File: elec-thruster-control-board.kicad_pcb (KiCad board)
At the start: 2 copper layers, 70 x 69 mm, 50 parts, among them J11 gp17-pwm0B, J12 gp2-pwm1A, J13 Conn_01x07, J15 gp6-pwm3A, J16 gp8-pwm4A, J18 gp19-pwm1B, J19 gp21-pwm2B, J2 gp0-pwm0A, J20 gp26-pwm5A, J21 gp27-pwm5B, J22 Conn_01x06, J24 Conn_01x06, J5 gp4-pwm2A

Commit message: This is the true final edition of this project
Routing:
- net /gp17-pwm0B: track 38.6 -> 52.9 mm
- net /gp0-pwm0A: track 40.4 -> 47.3 mm
- net /gp8-pwm4A: track 47.7 -> 48.2 mm
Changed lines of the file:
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@@
+	)
+	(segment
+		(start 163.58 81.58)
+		(end 164.75 82.75)
+		(width 0.4)
+		(layer "F.Cu")
+		(net 1)
 	)
 	(segment
@@
 	)
 	(segment
+		(start 164.75 92.25)
+		(end 162.5 94.5)
+		(width 0.4)
+		(layer "F.Cu")
+		(net 1)
+	)
+	(segment
+		(start 164.75 82.75)
+		(end 164.75 92.25)
+		(width 0.4)
+		(layer "F.Cu")
+		(net 1)
+	)
+	(segment
+		(start 162.5 94.5)
+		(end 150.6925 94.5)
+		(width 0.4)
+		(layer "F.Cu")
+		(net 1)
+	)
+	(segment
 		(start 151.285 96.715)
 		(end 152.5 95.5)
@@
 	)
 	(segment
-		(start 164.75 82.75)
+		(start 150.6925 94.5)
+		(end 148.4775 96.715)
+		(width 0.4)
+		(layer "F.Cu")
+		(net 1)
+	)
+	(segment
+		(start 162.25 81.58)
 		(end 163.58 81.58)
-		(width 0.4)
-		(layer "F.Cu")
-		(net 1)
-	)
-	(segment
-		(start 163.58 81.58)
-		(end 162.25 81.58)
 		(width 0.4)
 		(layer "F.Cu")
@@
 	)
 	(segment
-		(start 164.75 82.75)
-		(end 164.75 94)
-		(width 0.4)
-		(layer "F.Cu")
-		(net 1)
-	)
-	(segment
-		(start 164.75 94)
-		(end 163.25 95.5)
-		(width 0.4)
-		(layer "F.Cu")
-		(net 1)
-	)
-	(segment
 		(start 151.495 99.255)
 		(end 148.4775 99.255)
@@
 	(segment
 		(start 125.25 88.75)
-		(end 119.5 88.75)
+		(end 120.75 88.75)
 		(width 0.4)
 		(layer "F.Cu")
@@
 	(segment
 		(start 119.5 88.75)
-		(end 119.5 82.5)
+		(end 119.5 87.5)
 		(width 0.4)
 		(layer "F.Cu")
@@
 	)
 	(segment
+		(start 120.75 88.75)
+		(end 119.5 87.5)
+		(width 0.4)
+		(layer "F.Cu")
+		(net 6)
+	)
+	(segment
 		(start 127 87)
 		(end 125.25 88.75)
@@
 	)
 	(segment
+		(start 119.5 87.5)
+		(end 119.5 82.5)
+		(width 0.4)
+		(layer "F.Cu")
+		(net 6)
+	)
+	(segment
 		(start 127 80.5)
 		(end 127 87)
@@
 	)
 	(segment
+		(start 114.75 62)
+		(end 115.75 63)
+		(width 0.4)
+		(layer "F.Cu")
+		(net 7)
+	)
+	(segment
 		(start 116.75 60.5)
 		(end 116.75 70.46)
@@
 	)
 	(segment
-		(start 116.75 61)
-		(end 115.75 62)
-		(width 0.4)
-		(layer "F.Cu")
-		(net 7)
-	)
-	(segment
-		(start 115.75 62)
-		(end 109.75 62)
+		(start 109.75 62)
+		(end 114.75 62)
 		(width 0.4)
 		(layer "F.Cu")
@@
 	)
 	(segment
+		(start 115.75 69.46)
+		(end 116.75 70.46)
+		(width 0.4)
+		(layer "F.Cu")
+		(net 7)
+	)
+	(segment
 		(start 118.255 50.995)
 		(end 116.75 52.5)
@@
 	)
 	(segment
+		(start 115.75 63)
+		(end 115.75 69.46)
+		(width 0.4)
+		(layer "F.Cu")
+		(net 7)
+	)
+	(segment
 		(start 149.765 66.235)
 		(end 148.4775 66.235)
@@
 		(start 155.5 72)
 		(end 156.4375 72)
-		(width 0.2)
+		(width 0.4)
 		(layer "F.Cu")
 		(net 10)
@@
 		(start 156.4375 72)
 		(end 157.5 73.0625)
-		(width 0.2)
+		(width 0.4)
 		(layer "F.Cu")
 		(net 10)
@@
 	)
 	(segment
+		(start 164.54 79.04)
+		(end 165.5 80)
+		(width 0.4)
+		(layer "F.Cu")
+		(net 16)
+	)
+	(segment
 		(start 150.405 89.095)
 		(end 153.25 86.25)
@@
 	)
 	(segment
+		(start 162.25 79.04)
+		(end 164.54 79.04)
+		(width 0.4)
+		(layer "F.Cu")
+		(net 16)
+	)
+	(segment
 		(start 158.5 86.25)
 		(end 159.75 85)
@@
 	)
 	(segment
+		(start 161.21 79.04)
+		(end 162.25 79.04)
+		(width 0.4)
+		(layer "F.Cu")
+		(net 16)
+	)
+	(segment
+		(start 167 86.75)
+		(end 170.25 86.75)
+		(width 0.4)
+		(layer "F.Cu")
+		(net 16)
+	)
+	(segment
 		(start 165.5 85.25)
 		(end 167 86.75)
@@
 	)
 	(segment
-		(start 161.21 79.04)
-		(end 162.25 79.04)
-		(width 0.4)
-		(layer "F.Cu")
-		(net 16)
-	)
-	(segment
-		(start 165.04 79.04)
-		(end 165.5 79.5)
+		(start 165.5 80)
+		(end 165.5 85.25)
 		(width 0.4)
 		(layer "F.Cu")
@@
 	)
 	(segment
-		(start 162.25 79.04)
-		(end 165.04 79.04)
-		(width 0.4)
-		(layer "F.Cu")
-		(net 16)
-	)
-	(segment
 		(start 148.4775 89.095)
 		(end 150.405 89.095)
@@
 	)
 	(segment
-		(start 165.5 79.5)
-		(end 165.5 85.25)
-		(width 0.4)
-		(layer "F.Cu")
-		(net 16)
-	)
-	(segment
-		(start 167 86.75)
-		(end 170.25 86.75)
-		(width 0.4)
-		(layer "F.Cu")
-		(net 16)
-	)
-	(segment
 		(start 134.015 84.015)
 		(end 146.75 96.75)
@@
 	)
 	(segment
+		(start 151.0425 68.75)
+		(end 159.58 68.75)
+		(width 0.4)
+		(layer "F.Cu")
+		(net 25)
+	)
+	(segment
+		(start 162.25 71.42)
+		(end 159.58 68.75)
+		(width 0.4)
+		(layer "F.Cu")
+		(net 25)
+	)
+	(segment
 		(start 162.25 65.75)
 		(end 162.25 71.42)
@@
 	(segment
 		(start 148.4775 71.315)
-		(end 154.0425 65.75)
-		(width 0.4)
-		(layer "F.Cu")
-		(net 25)
-	)
-	(segment
-		(start 154.0425 65.75)
-		(end 162.25 65.75)
+		(end 151.0425 68.75)
 		(width 0.4)
 		(layer "F.Cu")
@@
 	)
 	(segment
-		(start 157.475 75.9125)
-		(end 157.5 75.9375)
-		(width 0.2)
-		(layer "F.Cu")
-		(net 41)
-	)
-	(segment
 		(start 153.75 74.9125)
 		(end 157.475 74.9125)
-		(width 0.2)
+		(width 0.4)
 		(layer "F.Cu")
 		(net 41)

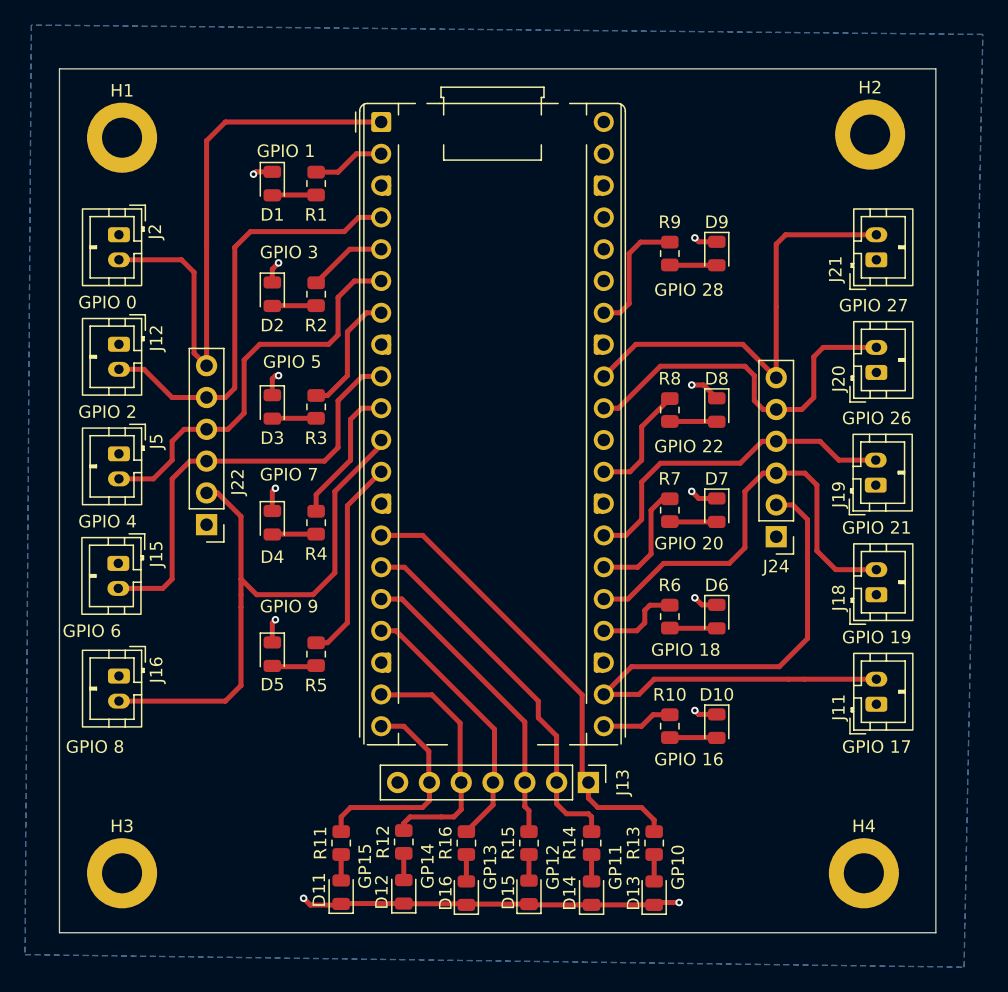
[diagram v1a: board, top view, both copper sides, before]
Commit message: Updated footprints in the schematic and pcb design. Also cleaned up some of the routing.
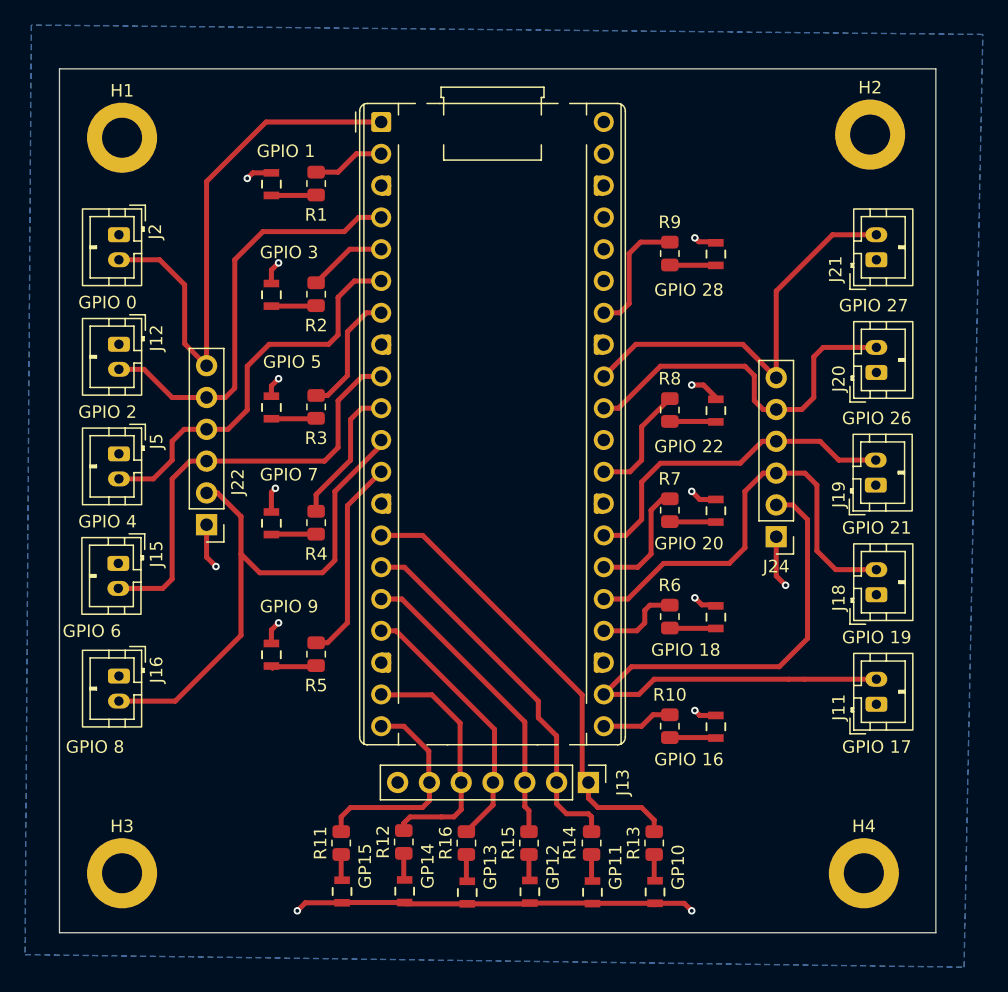
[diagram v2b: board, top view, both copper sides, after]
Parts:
- D1, D10, D11, D12, D13, D14, D15, D16, D2, D3, D4, D5, D6, D7, D8, D9: footprint LED_SMD:LED_0805_2012Metric -> Imported Footprints:LED_APT2012LZGCK
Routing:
- net GND: track 50.0 -> 60.1 mm, vias 12 -> 14
- net /gp8-pwm4A: track 48.2 -> 44.6 mm
- net /gp0-pwm0A: track 47.3 -> 43.9 mm
- net /gp27-pwm5B: track 34.9 -> 32.7 mm
- net Net-(D3-A): track 4.26 -> 3.62 mm
- net Net-(D2-A): track 4.26 -> 3.62 mm
- net /gp2-pwm1A: track 34.4 -> 33.8 mm

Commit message: Final PCB Design after design review Updated dimensions of board and mounting hole distance Fixed LED footprint Added Measurement values
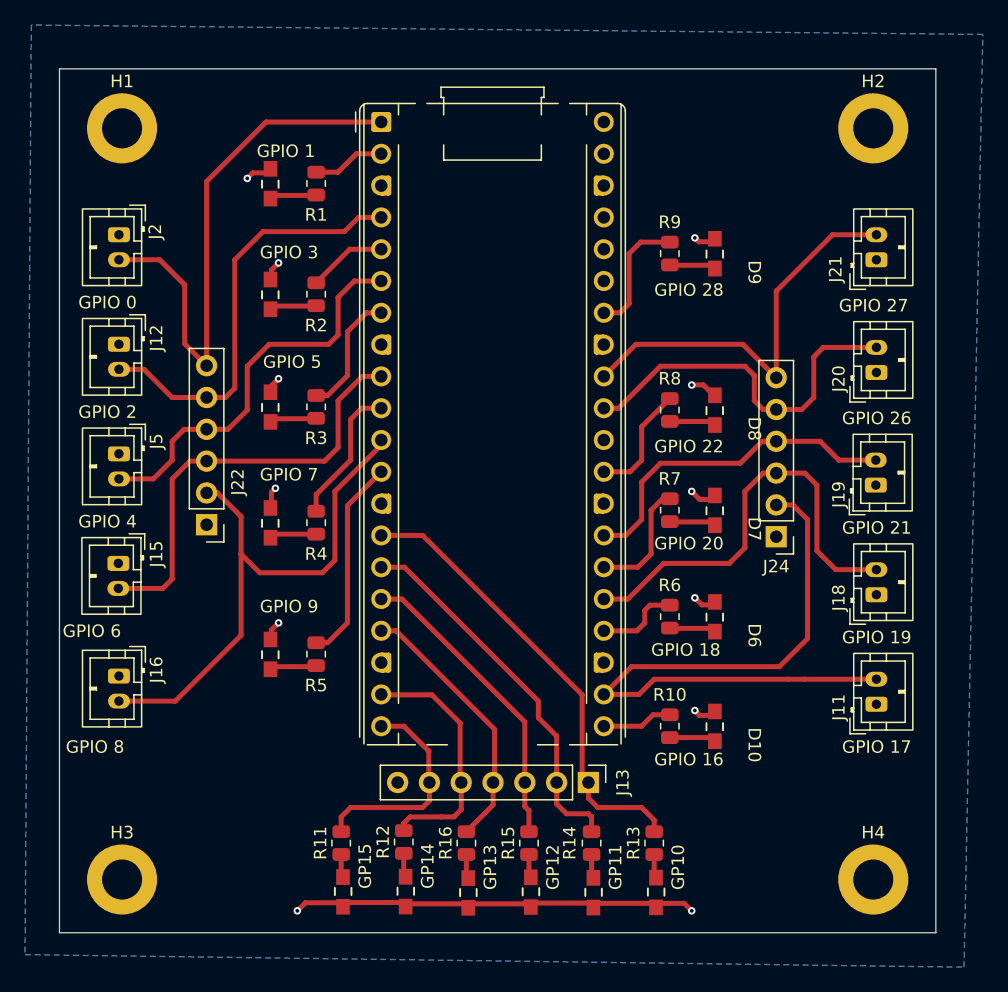
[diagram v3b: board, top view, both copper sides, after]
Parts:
- moved H4 0.90 mm to (170.0, 111.5)
- moved H1 0.75 mm to (110.0, 51.5)
- moved H2 0.56 mm to (170.0, 51.5)
- moved H3 0.50 mm to (110.0, 111.5)
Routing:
- net GND: track 60.1 -> 52.3 mm, vias 14 -> 12

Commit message: Added Labels for LEDs, and corrected Labels
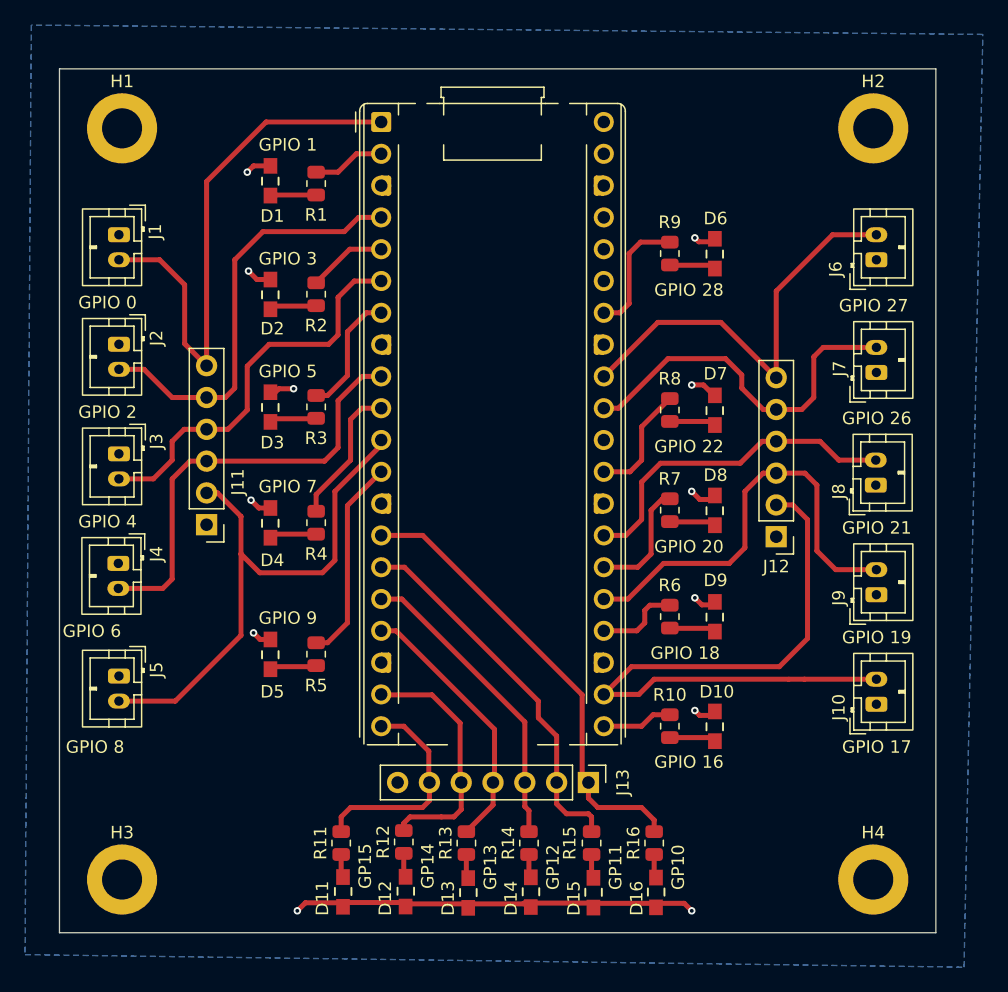
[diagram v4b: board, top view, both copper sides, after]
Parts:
- moved D1 0.24 mm to (122.0, 55.7)
- renumbered D16 to D13, D15 to D14, D14 to D15, D13 to D16, D9 to D6, D8 to D7, D7 to D8, D6 to D9, J2 to J1, J11 to J10, J22 to J11, J24 to J12, J12 to J2, J5 to J3, J15 to J4, J16 to J5, J21 to J6, J20 to J7, J19 to J8, J18 to J9, R16 to R13, R15 to R14, R14 to R15, R13 to R16
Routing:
- net /gp27-pwm5B: track 32.7 -> 34.2 mm
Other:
- board text removed: "J20"

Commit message: Minor fix
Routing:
- net /gp17-pwm0B: track 52.9 -> 38.9 mm
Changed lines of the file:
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@@
+	)
+	(segment
+		(start 150.3925 94.8)
+		(end 148.4775 96.715)
+		(width 0.4)
+		(layer "F.Cu")
+		(net 1)
 	)
 	(segment
@@
 	)
 	(segment
-		(start 152.5 95.5)
-		(end 163.25 95.5)
+		(start 162.2 94.8)
+		(end 162.4 94.8)
 		(width 0.4)
 		(layer "F.Cu")
@@
 	)
 	(segment
-		(start 162.5 94.5)
-		(end 150.6925 94.5)
+		(start 162.2 94.8)
+		(end 150.3925 94.8)
 		(width 0.4)
 		(layer "F.Cu")
@@
 	)
 	(segment
-		(start 151.285 96.715)
-		(end 152.5 95.5)
+		(start 163.1 95.5)
+		(end 170.25 95.5)
 		(width 0.4)
 		(layer "F.Cu")
@@
 	)
 	(segment
-		(start 150.6925 94.5)
-		(end 148.4775 96.715)
+		(start 162.5 94.5)
+		(end 162.2 94.8)
+		(width 0.4)
+		(layer "F.Cu")
+		(net 1)
+	)
+	(segment
+		(start 162.4 94.8)
+		(end 163.1 95.5)
 		(width 0.4)
 		(layer "F.Cu")
@@
 		(width 0.4)
 		(layer "F.Cu")
-		(net 1)
-	)
-	(segment
-		(start 164.5 95.5)
-		(end 170.25 95.5)
-		(width 0.4)
-		(layer "F.Cu")
-		(net 1)
-	)
-	(segment
-		(start 163.25 95.5)
-		(end 164.5 95.5)
-		(width 0.4)
-		(layer "F.Cu")
-		(net 1)
-	)
-	(segment
-		(start 148.4775 96.715)
-		(end 151.285 96.715)
-		(width 0.4)
-		(layer "F.Cu")

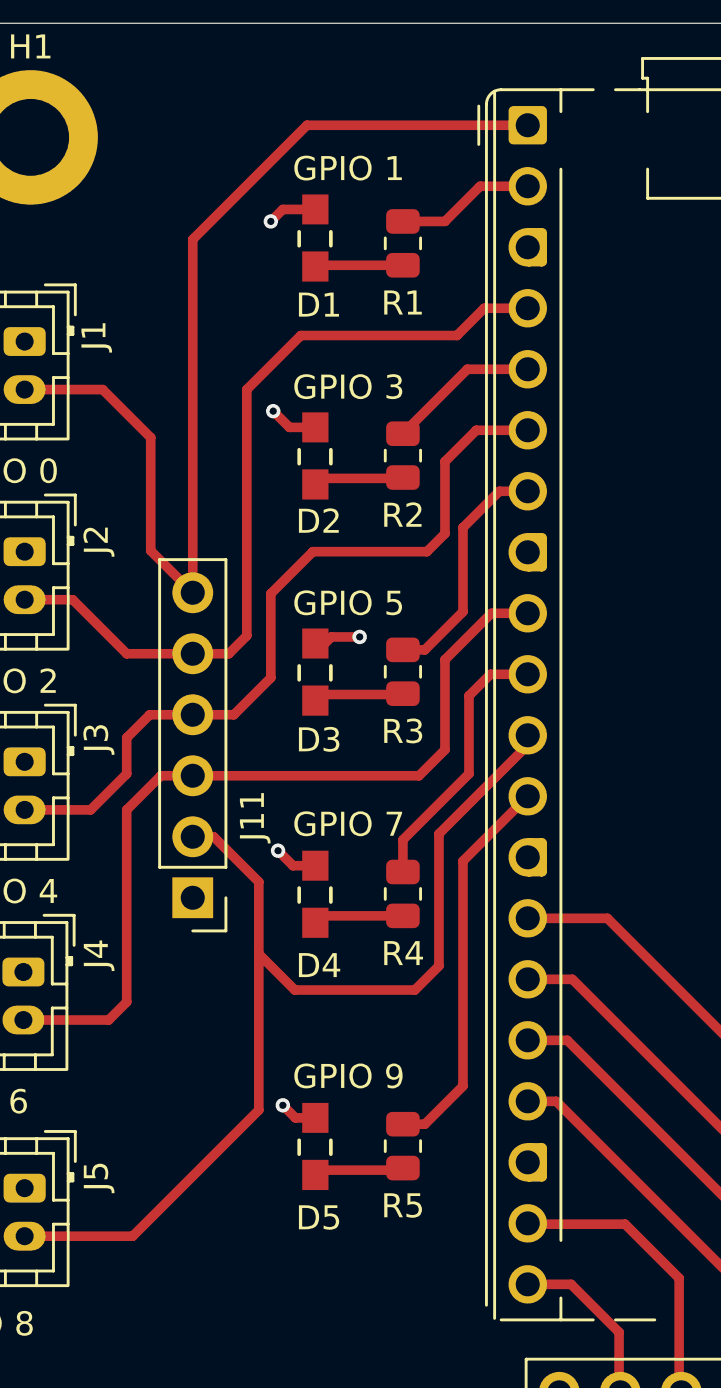
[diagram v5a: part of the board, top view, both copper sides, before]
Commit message: Moved left LEDs closer to pico
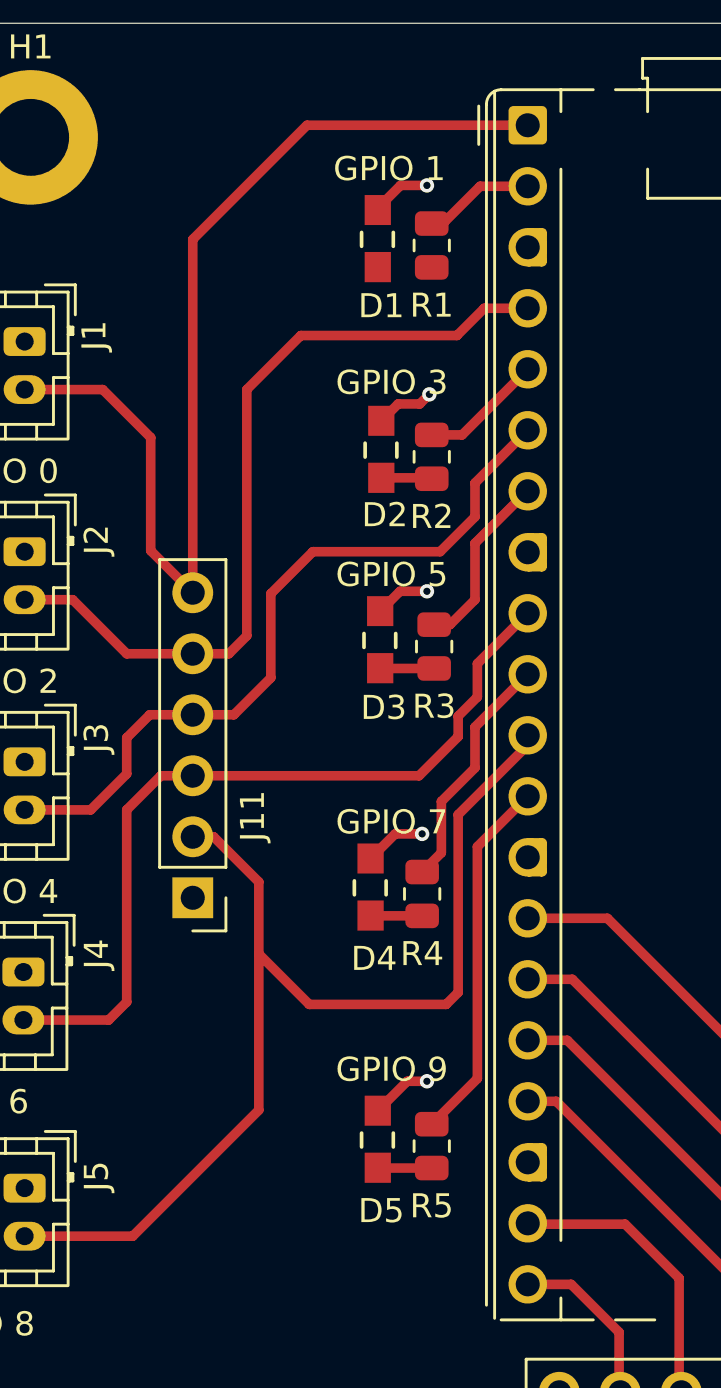
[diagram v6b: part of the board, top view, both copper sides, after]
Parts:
- moved D3 3.02 mm to (124.7, 72.4)
- moved D2 2.76 mm to (124.7, 64.5)
- moved D5 2.62 mm to (124.6, 93.2)
- moved D1 2.60 mm to (124.6, 55.7)
- moved D4 2.32 mm to (124.3, 82.7)
- moved R3 1.67 mm to (126.8, 72.7)
- moved R1 1.20 mm to (126.7, 56.0)
- moved R2 1.20 mm to (126.7, 64.8)
- moved R5 1.20 mm to (126.7, 93.5)
- moved R4 0.80 mm to (126.3, 83.0)
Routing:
- net Net-(D1-A): track 3.75 -> 0.00 mm
- net GND: track 52.2 -> 55.5 mm
- net Net-(A1-GPIO5): track 9.98 -> 7.57 mm
- net /gp8-pwm4A: track 44.6 -> 46.2 mm
- net Net-(D5-A): track 3.67 -> 2.25 mm
- net Net-(A1-GPIO1): track 5.80 -> 4.40 mm
- net Net-(D3-A): track 3.62 -> 2.25 mm
- net Net-(D4-A): track 3.51 -> 2.15 mm
- net Net-(A1-GPIO9): track 16.6 -> 15.3 mm
- net Net-(A1-GPIO3): track 6.40 -> 5.13 mm
- net Net-(A1-GPIO7): track 11.3 -> 10.1 mm
- net Net-(D2-A): track 3.62 -> 2.45 mm
- net /gp4-pwm2A: track 32.2 -> 31.2 mm
- net /gp6-pwm3A: track 35.4 -> 34.5 mm
